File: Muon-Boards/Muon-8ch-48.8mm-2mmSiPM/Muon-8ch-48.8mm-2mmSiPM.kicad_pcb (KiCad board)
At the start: 4 copper layers, 420.4 x 48.8 mm, 21 parts

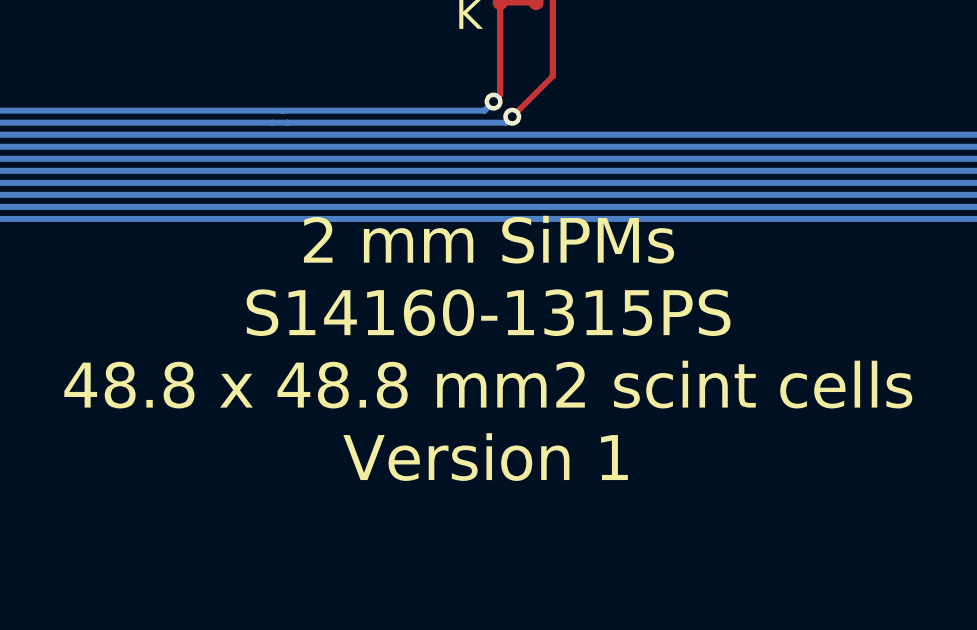
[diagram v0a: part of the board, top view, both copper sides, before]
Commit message: Updated silkscreen with proper SiPM number S13360-2050VE
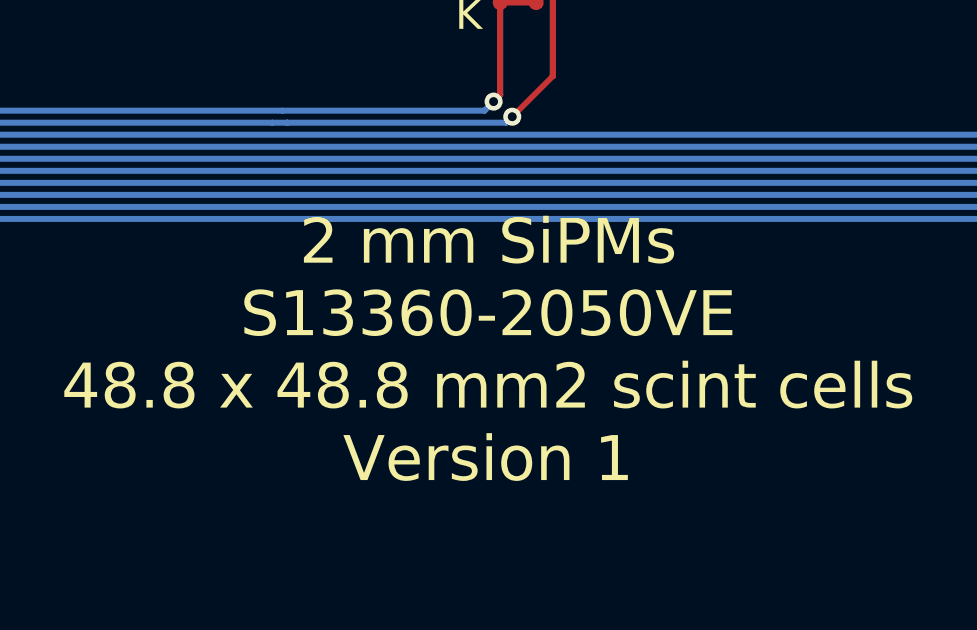
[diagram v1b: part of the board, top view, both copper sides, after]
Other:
- board text added: "2 mm SiPMs S13360-2050VE 48.8 x 48.8 mm2 scint cells Version 1"
- board text removed: "2 mm SiPMs S14160-1315PS 48.8 x 48.8 mm2 scint cells Version 1"
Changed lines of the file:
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@@
 		)
 	)
-	(gr_text "2 mm SiPMs\nS14160-1315PS\n48.8 x 48.8 mm2 scint cells\nVersion 1"
+	(gr_text "2 mm SiPMs\nS13360-2050VE\n48.8 x 48.8 mm2 scint cells\nVersion 1"
 		(at 182.7 95.2 0)
 		(layer "F.SilkS")
